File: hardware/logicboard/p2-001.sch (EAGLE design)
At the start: 33 parts, among them IC1 5V, IC2 74LS07N, IC3 4066N, IC4 LTC485N, K1 G5V1, T1 2SC1815, U1 DS18B20

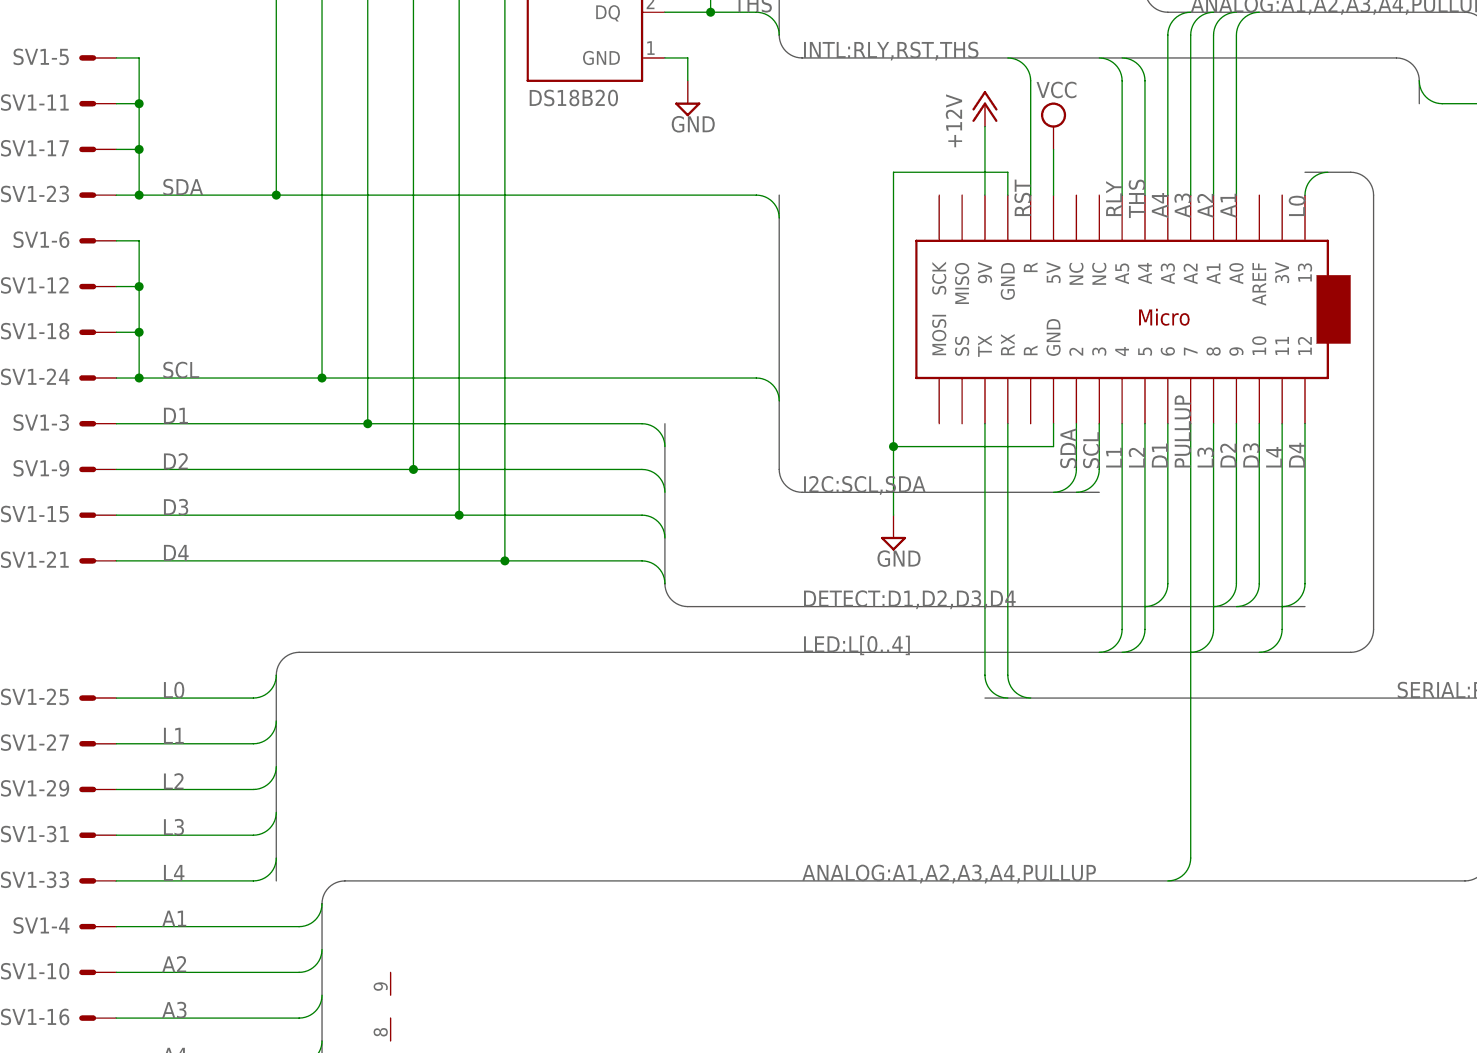
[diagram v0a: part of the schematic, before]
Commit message: Fixed unconnected wires.
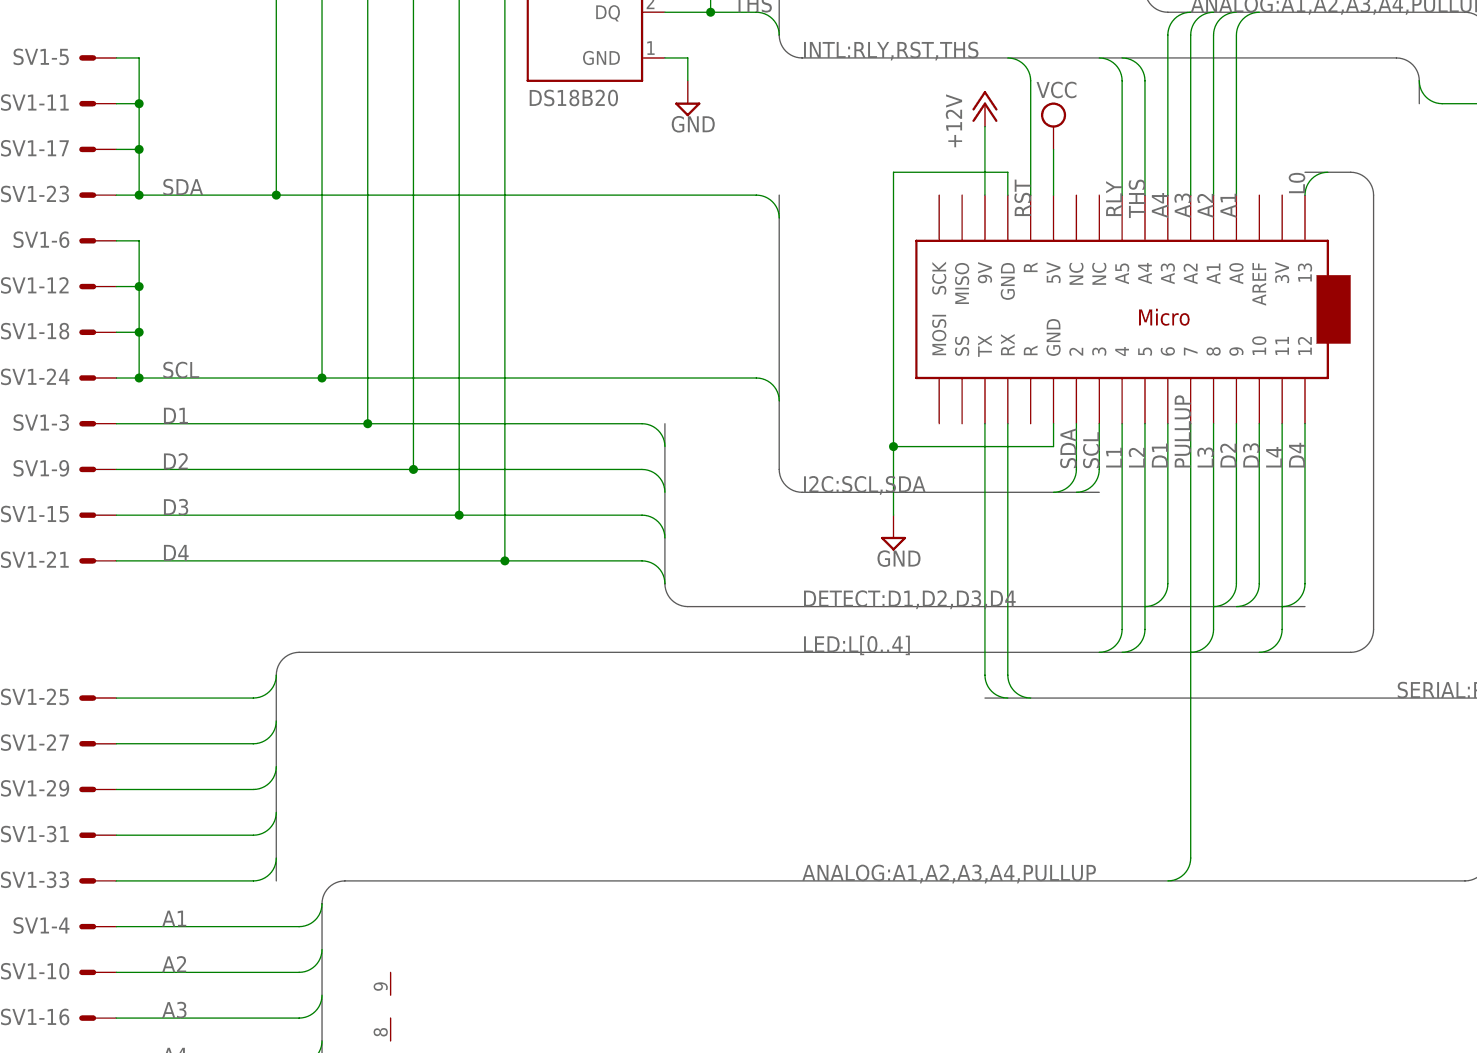
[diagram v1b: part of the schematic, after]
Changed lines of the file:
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@@
 <setting verticaltext="up"/>
 </settings>
-<grid distance="0.1" unitdist="inch" unit="inch" style="lines" multiple="1" display="no" altdistance="0.01" altunitdist="inch" altunit="inch"/>
+<grid distance="0.1" unitdist="inch" unit="inch" style="lines" multiple="1" display="yes" altdistance="0.01" altunitdist="inch" altunit="inch"/>
 <layers>
 <layer number="1" name="Top" color="4" fill="1" visible="no" active="no"/>
@@
 </segment>
 </net>
-<net name="L0" class="0">
-<segment>
-<pinref part="MC1" gate="G$1" pin="13"/>
-<wire x1="160.02" y1="160.02" x2="157.48" y2="157.48" width="0.1524" layer="91" curve="90"/>
-<label x="157.48" y="154.94" size="1.778" layer="95" rot="R90"/>
-</segment>
-<segment>
-<wire x1="40.64" y1="101.6" x2="25.4" y2="101.6" width="0.1524" layer="91"/>
-<pinref part="SV1" gate="-25" pin="S"/>
-<label x="30.48" y="101.6" size="1.778" layer="95"/>
-<wire x1="43.18" y1="104.14" x2="40.64" y2="101.6" width="0.1524" layer="91" curve="-90"/>
-</segment>
-</net>
-<net name="L1" class="0">
-<segment>
-<pinref part="MC1" gate="G$1" pin="4"/>
-<wire x1="134.62" y1="106.68" x2="137.16" y2="109.22" width="0.1524" layer="91" curve="90"/>
-<wire x1="137.16" y1="109.22" x2="137.16" y2="132.08" width="0.1524" layer="91"/>
-<label x="137.16" y="127" size="1.778" layer="95" rot="R90"/>
-</segment>
-<segment>
-<pinref part="SV1" gate="-27" pin="S"/>
-<wire x1="40.64" y1="96.52" x2="25.4" y2="96.52" width="0.1524" layer="91"/>
-<label x="30.48" y="96.52" size="1.778" layer="95"/>
-<wire x1="43.18" y1="99.06" x2="40.64" y2="96.52" width="0.1524" layer="91" curve="-90"/>
-</segment>
-</net>
-<net name="L2" class="0">
-<segment>
-<pinref part="SV1" gate="-29" pin="S"/>
-<wire x1="40.64" y1="91.44" x2="25.4" y2="91.44" width="0.1524" layer="91"/>
-<label x="30.48" y="91.44" size="1.778" layer="95"/>
-<wire x1="43.18" y1="93.98" x2="40.64" y2="91.44" width="0.1524" layer="91" curve="-90"/>
-</segment>
-<segment>
-<pinref part="MC1" gate="G$1" pin="5"/>
-<wire x1="137.16" y1="106.68" x2="139.7" y2="109.22" width="0.1524" layer="91" curve="90"/>
-<wire x1="139.7" y1="109.22" x2="139.7" y2="132.08" width="0.1524" layer="91"/>
-<label x="139.7" y="127" size="1.778" layer="95" rot="R90"/>
-</segment>
-</net>
-<net name="L3" class="0">
-<segment>
-<pinref part="MC1" gate="G$1" pin="8"/>
-<wire x1="144.78" y1="106.68" x2="147.32" y2="109.22" width="0.1524" layer="91" curve="90"/>
-<wire x1="147.32" y1="109.22" x2="147.32" y2="132.08" width="0.1524" layer="91"/>
-<label x="147.32" y="127" size="1.778" layer="95" rot="R90"/>
-</segment>
-<segment>
-<pinref part="SV1" gate="-31" pin="S"/>
-<wire x1="40.64" y1="86.36" x2="25.4" y2="86.36" width="0.1524" layer="91"/>
-<label x="30.48" y="86.36" size="1.778" layer="95"/>
-<wire x1="43.18" y1="88.9" x2="40.64" y2="86.36" width="0.1524" layer="91" curve="-90"/>
-</segment>
-</net>
 <net name="L4" class="0">
 <segment>
@@
 <segment>
 <pinref part="SV1" gate="-33" pin="S"/>
+<wire x1="43.18" y1="83.82" x2="40.64" y2="81.28" width="0.1524" layer="91" curve="-90"/>
 <wire x1="40.64" y1="81.28" x2="25.4" y2="81.28" width="0.1524" layer="91"/>
-<label x="30.48" y="81.28" size="1.778" layer="95"/>
-<wire x1="43.18" y1="83.82" x2="40.64" y2="81.28" width="0.1524" layer="91" curve="-90"/>
 </segment>
 </net>
@@
 </segment>
 </net>
+<net name="L1" class="0">
+<segment>
+<pinref part="MC1" gate="G$1" pin="4"/>
+<wire x1="134.62" y1="106.68" x2="137.16" y2="109.22" width="0.1524" layer="91" curve="90"/>
+<wire x1="137.16" y1="109.22" x2="137.16" y2="132.08" width="0.1524" layer="91"/>
+<label x="137.16" y="127" size="1.778" layer="95" rot="R90"/>
+</segment>
+<segment>
+<pinref part="SV1" gate="-27" pin="S"/>
+<wire x1="43.18" y1="99.06" x2="40.64" y2="96.52" width="0.1524" layer="91" curve="-90"/>
+<wire x1="40.64" y1="96.52" x2="25.4" y2="96.52" width="0.1524" layer="91"/>
+</segment>
+</net>
+<net name="L2" class="0">
+<segment>
+<pinref part="MC1" gate="G$1" pin="5"/>
+<wire x1="137.16" y1="106.68" x2="139.7" y2="109.22" width="0.1524" layer="91" curve="90"/>
+<wire x1="139.7" y1="109.22" x2="139.7" y2="132.08" width="0.1524" layer="91"/>
+<label x="139.7" y="127" size="1.778" layer="95" rot="R90"/>
+</segment>
+<segment>
+<pinref part="SV1" gate="-29" pin="S"/>
+<wire x1="43.18" y1="93.98" x2="40.64" y2="91.44" width="0.1524" layer="91" curve="-90"/>
+<wire x1="40.64" y1="91.44" x2="25.4" y2="91.44" width="0.1524" layer="91"/>
+</segment>
+</net>
+<net name="L3" class="0">
+<segment>
+<pinref part="MC1" gate="G$1" pin="8"/>
+<wire x1="144.78" y1="106.68" x2="147.32" y2="109.22" width="0.1524" layer="91" curve="90"/>
+<wire x1="147.32" y1="109.22" x2="147.32" y2="132.08" width="0.1524" layer="91"/>
+<label x="147.32" y="127" size="1.778" layer="95" rot="R90"/>
+</segment>
+<segment>
+<pinref part="SV1" gate="-31" pin="S"/>
+<wire x1="43.18" y1="88.9" x2="40.64" y2="86.36" width="0.1524" layer="91" curve="-90"/>
+<wire x1="40.64" y1="86.36" x2="25.4" y2="86.36" width="0.1524" layer="91"/>
+</segment>
+</net>
+<net name="L0" class="0">
+<segment>
+<pinref part="MC1" gate="G$1" pin="13"/>
+<wire x1="160.02" y1="160.02" x2="157.48" y2="157.48" width="0.1524" layer="91" curve="90"/>
+<label x="157.48" y="157.48" size="1.778" layer="95" rot="R90"/>
+</segment>
+<segment>
+<pinref part="SV1" gate="-25" pin="S"/>
+<wire x1="43.18" y1="104.14" x2="40.64" y2="101.6" width="0.1524" layer="91" curve="-90"/>
+<wire x1="40.64" y1="101.6" x2="25.4" y2="101.6" width="0.1524" layer="91"/>
+</segment>
+</net>

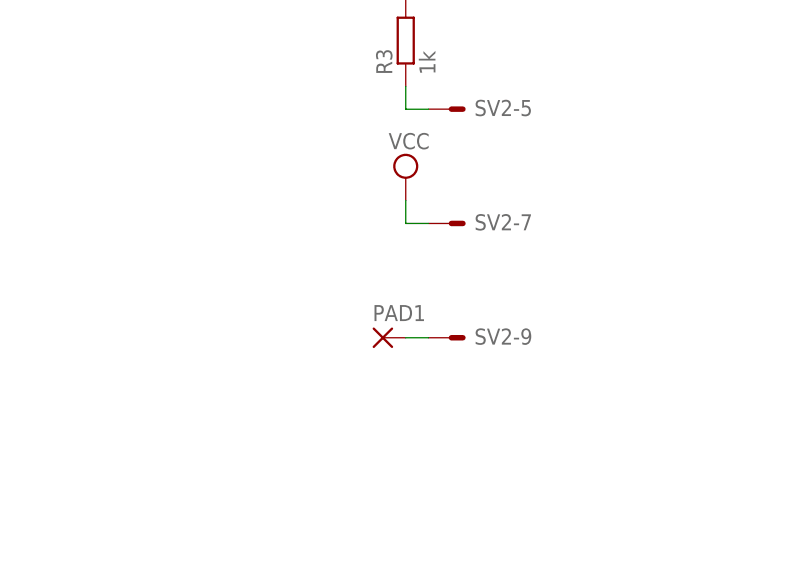
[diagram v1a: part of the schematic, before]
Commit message: Now pin 3 of MIDI In is connected to Vcc.
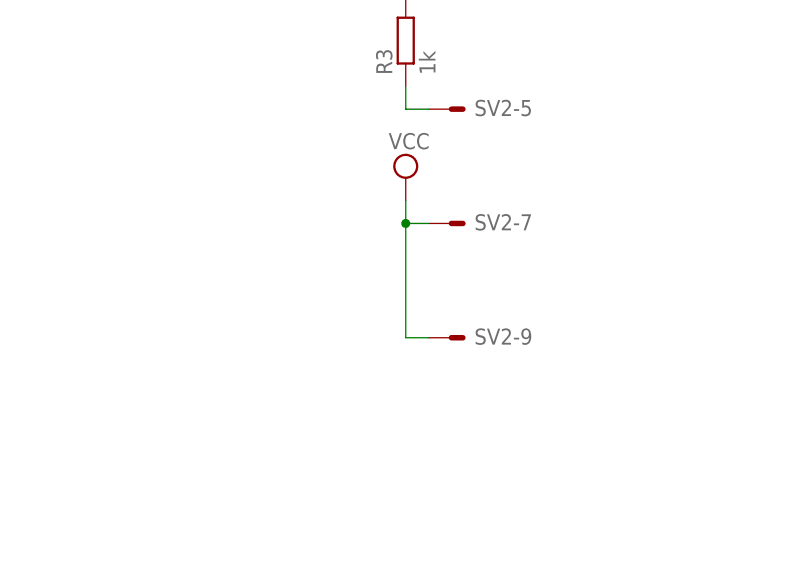
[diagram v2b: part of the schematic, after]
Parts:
- removed PAD1: (no value), wirepad:1,6/0,8
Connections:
- removed net N$1: PAD1.P, SV2-9.S
- net VCC: now also SV2-9.S
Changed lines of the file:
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@@
 <setting verticaltext="up"/>
 </settings>
-<grid distance="0.1" unitdist="inch" unit="inch" style="lines" multiple="1" display="yes" altdistance="0.01" altunitdist="inch" altunit="inch"/>
+<grid distance="0.1" unitdist="inch" unit="inch" style="lines" multiple="1" display="no" altdistance="0.01" altunitdist="inch" altunit="inch"/>
 <layers>
 <layer number="1" name="Top" color="4" fill="1" visible="no" active="no"/>
@@
 <part name="SUPPLY30" library="supply2" deviceset="GND" device=""/>
 <part name="R4" library="resistor" library_urn="urn:adsk.eagle:library:348" deviceset="R-EU_" device="0204/5" package3d_urn="urn:adsk.eagle:package:23488/1" value="120"/>
-<part name="PAD1" library="wirepad" library_urn="urn:adsk.eagle:library:412" deviceset="1,6/0,8" device="" package3d_urn="urn:adsk.eagle:package:30830/1"/>
 </parts>
 <sheets>
@@
 <attribute name="NAME" x="227.33" y="77.6986" size="1.778" layer="95"/>
 <attribute name="VALUE" x="227.33" y="72.898" size="1.778" layer="96"/>
-</instance>
-<instance part="PAD1" gate="P" x="243.84" y="208.28" smashed="yes">
-<attribute name="NAME" x="242.697" y="210.1342" size="1.778" layer="95"/>
-<attribute name="VALUE" x="242.697" y="204.978" size="1.778" layer="96"/>
 </instance>
 </instances>
@@
 <pinref part="SV2" gate="-7" pin="S"/>
 <wire x1="248.92" y1="220.98" x2="246.38" y2="220.98" width="0.1524" layer="91"/>
+<wire x1="246.38" y1="220.98" x2="246.38" y2="208.28" width="0.1524" layer="91"/>
+<junction x="246.38" y="220.98"/>
+<pinref part="SV2" gate="-9" pin="S"/>
+<wire x1="246.38" y1="208.28" x2="248.92" y2="208.28" width="0.1524" layer="91"/>
 </segment>
 <segment>
@@
 </segment>
 </net>
-<net name="N$1" class="0">
-<segment>
-<pinref part="SV2" gate="-9" pin="S"/>
-<pinref part="PAD1" gate="P" pin="P"/>
-<wire x1="246.38" y1="208.28" x2="248.92" y2="208.28" width="0.1524" layer="91"/>
-</segment>
-</net>

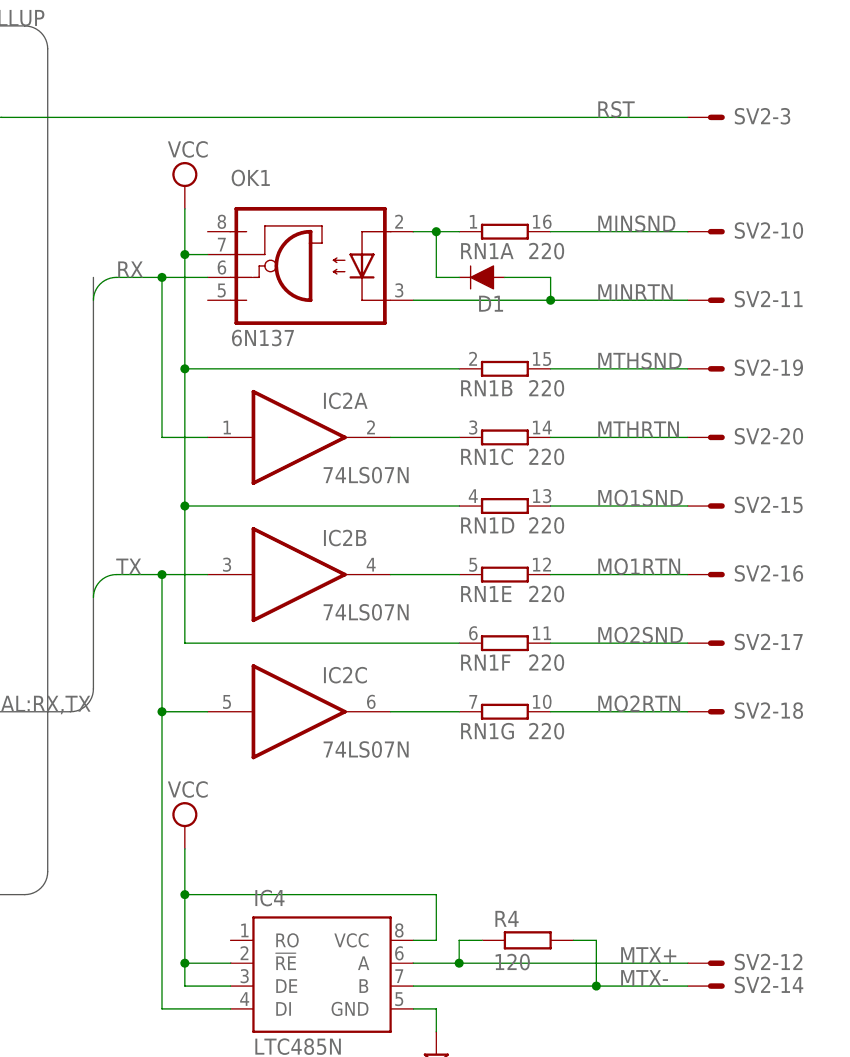
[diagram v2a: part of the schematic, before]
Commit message: Fixed connection of TLP552 to the power pins.
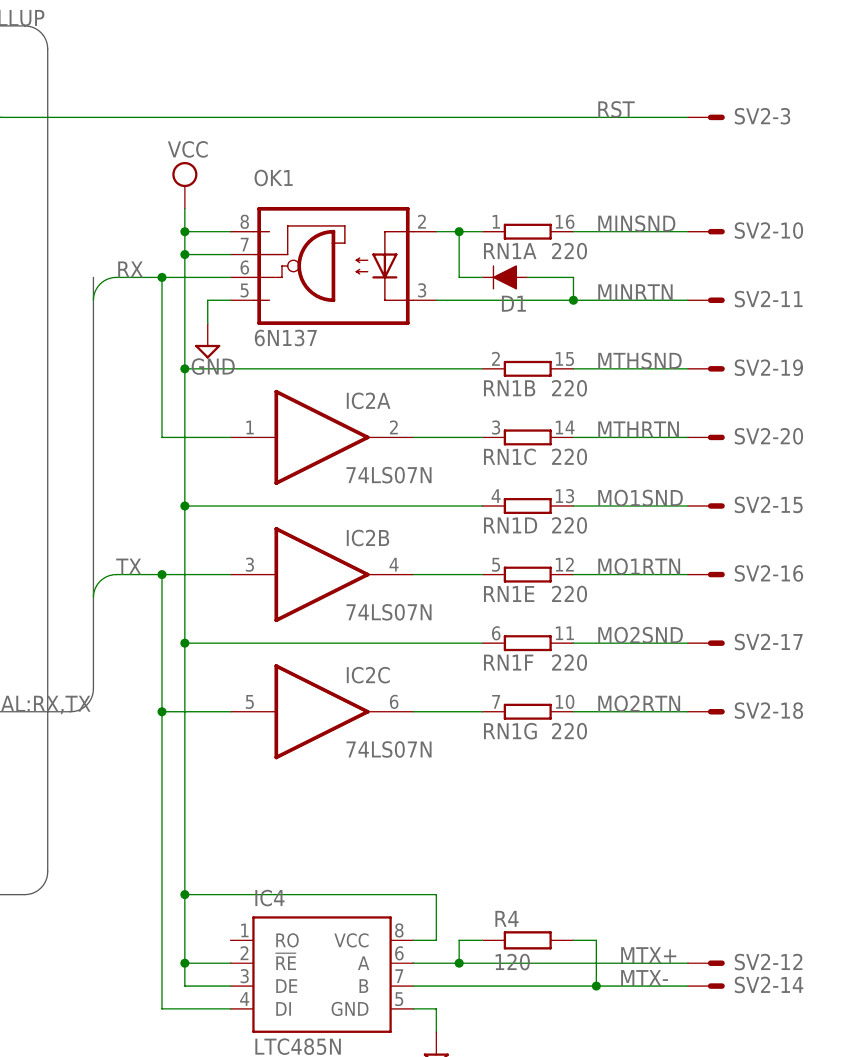
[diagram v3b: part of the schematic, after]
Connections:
- net GND: now also OK1.GND
- net VCC: now also OK1.VCC
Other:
- moved on the sheet: D1, IC2A, IC2B, IC2C, OK1, RN1A, RN1B, RN1C, RN1D, RN1E, RN1F, RN1G

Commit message: Moved Arduino Micro downward.
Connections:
- net +12V renamed VIN
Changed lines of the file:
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@@
 </segment>
 </net>
-<net name="+12V" class="2">
+<net name="VIN" class="2">
 <segment>
 <pinref part="MC1" gate="G$1" pin="9V"/>
